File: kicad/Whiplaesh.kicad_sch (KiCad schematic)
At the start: 74 parts, among them SW1 SW_PUSH, SW10 SW_PUSH, SW11 SW_PUSH, SW12 SW_PUSH, SW13 SW_PUSH, SW14 SW_PUSH, SW15 SW_PUSH, SW16 SW_PUSH, SW17 SW_PUSH, SW18 SW_PUSH, SW19 SW_PUSH, SW2 SW_PUSH, SW20 SW_PUSH, SW21 SW_PUSH, SW22 SW_PUSH, SW23 SW_PUSH, SW24 SW_PUSH, SW25 SW_PUSH, SW26 SW_PUSH, SW27 SW_PUSH, SW28 SW_PUSH, SW29 SW_PUSH, SW3 SW_PUSH, SW30 SW_PUSH, SW31 SW_PUSH, SW32 SW_PUSH, SW4 SW_PUSH, SW5 SW_PUSH, SW6 SW_PUSH, SW7 SW_PUSH, SW8 SW_PUSH, SW9 SW_PUSH

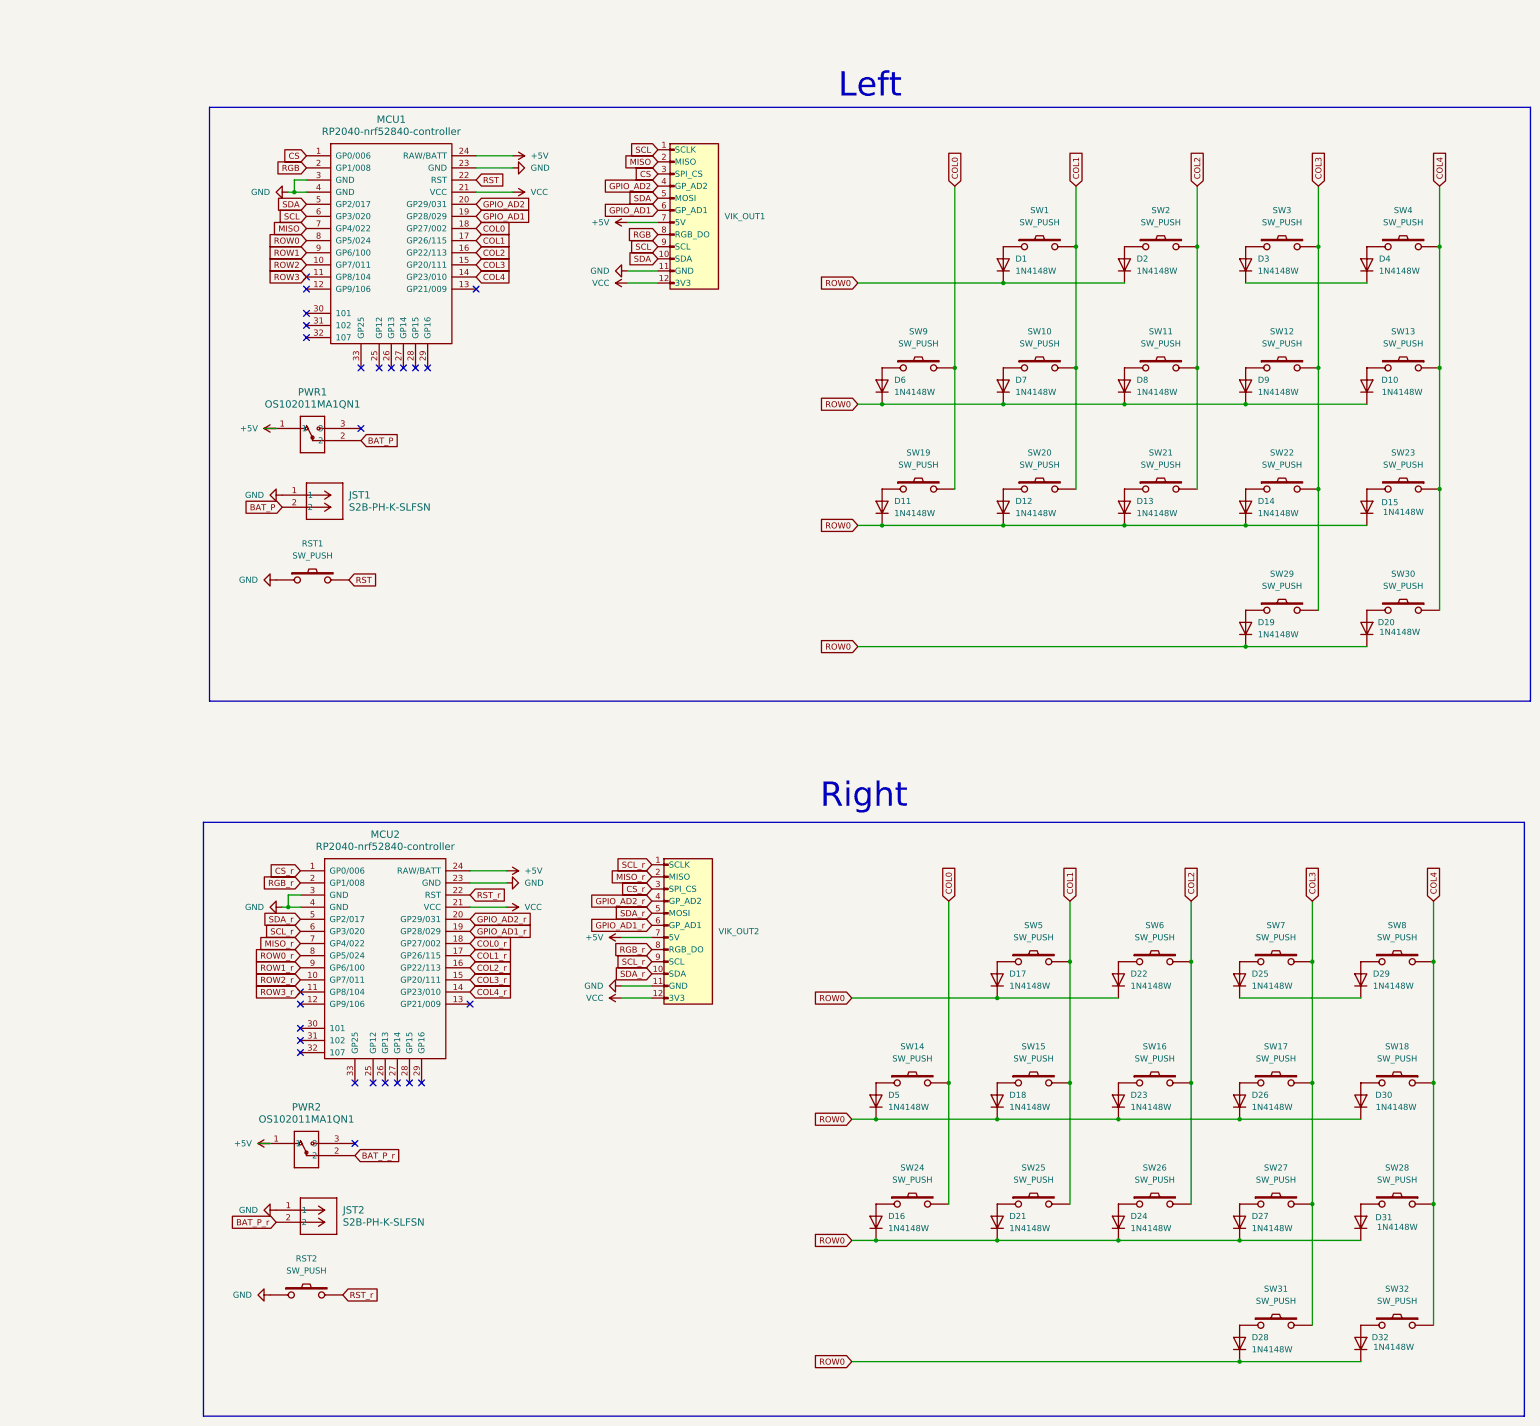
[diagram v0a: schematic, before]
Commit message: Add missing connections, fix diodes references, fix shared pins on vik connector
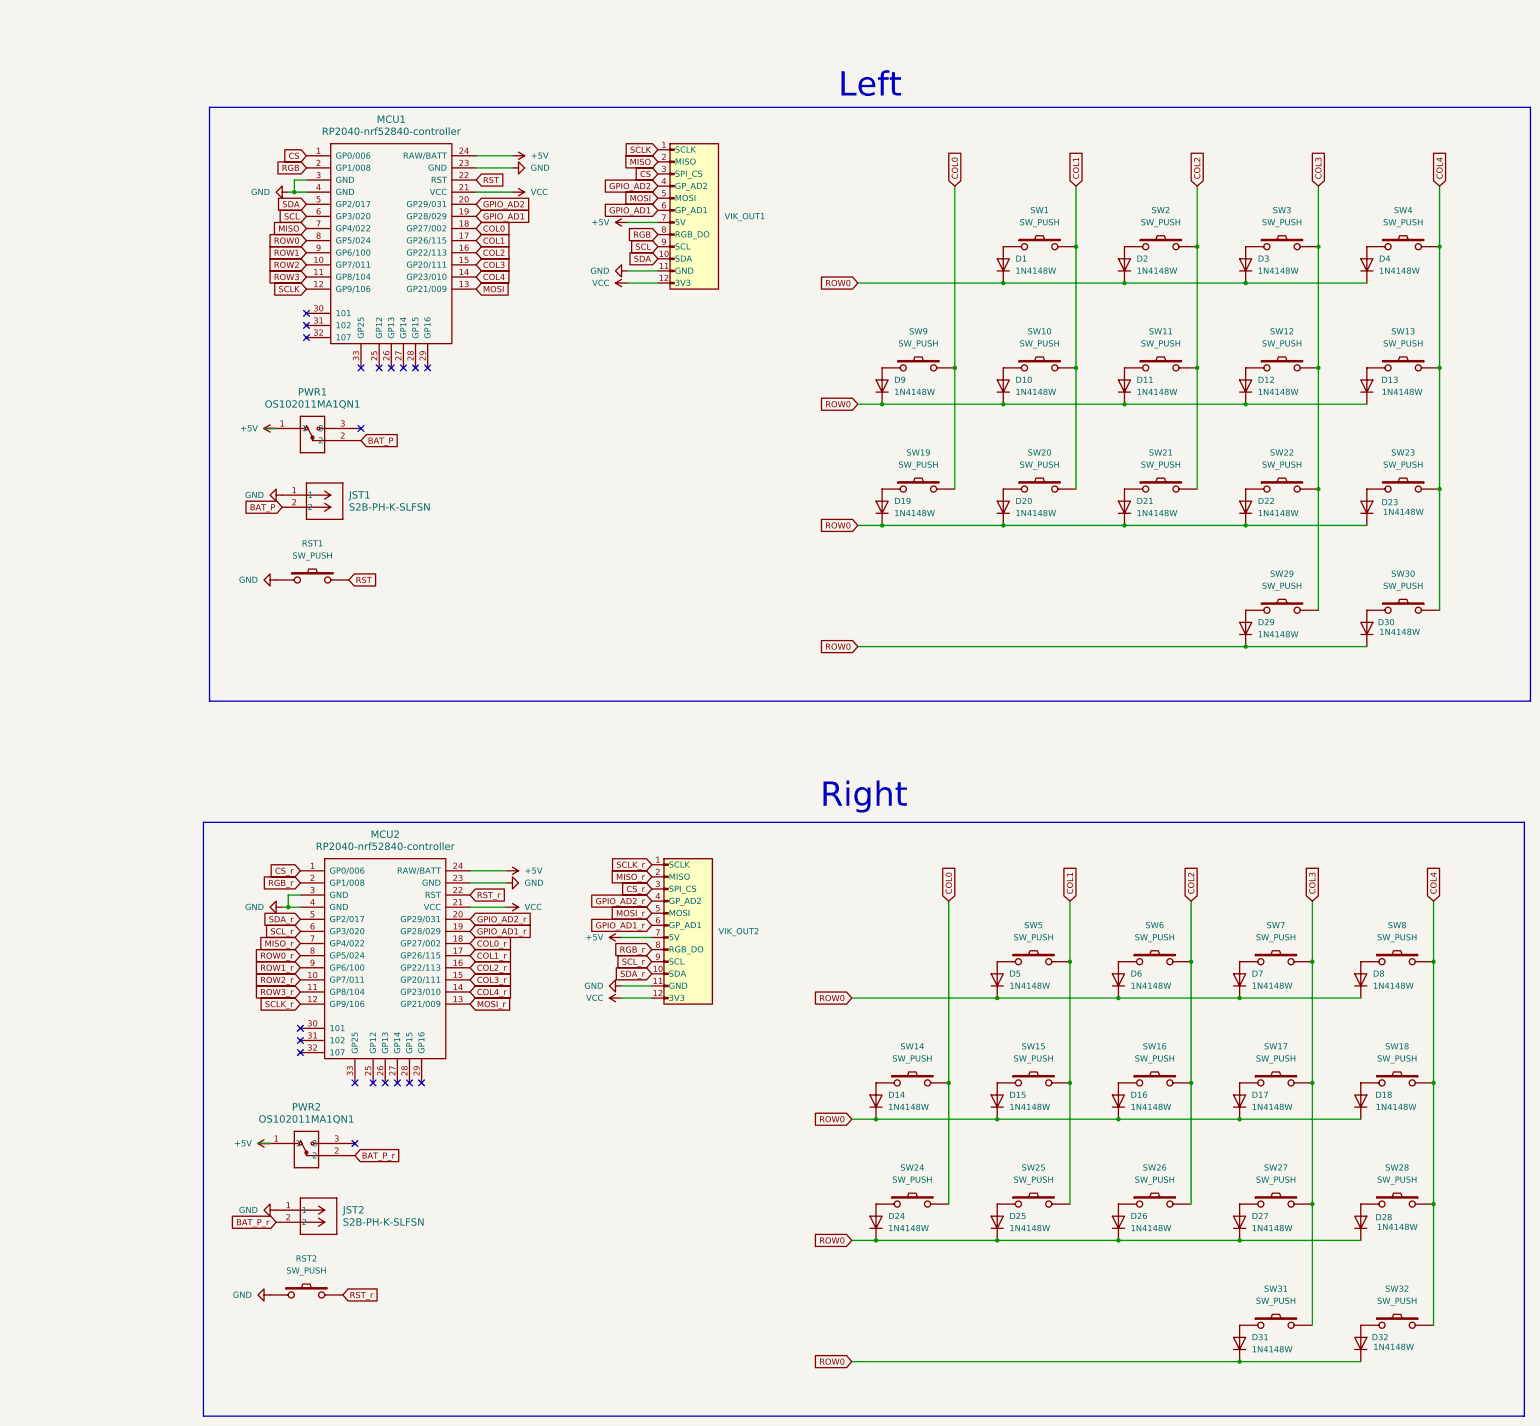
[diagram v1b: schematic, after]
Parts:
- renumbered D7 to D10, D8 to D11, D9 to D12, D10 to D13, D5 to D14, D18 to D15, D23 to D16, D26 to D17, D30 to D18, D11 to D19, D12 to D20, D13 to D21, D14 to D22, D15 to D23, D16 to D24, D21 to D25, D24 to D26, D31 to D28, D19 to D29, D20 to D30, D28 to D31, D17 to D5, D22 to D6, D25 to D7, D29 to D8, D6 to D9
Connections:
- net ROW0: now also D3.1 (K), D4.1 (K), D7.1 (K), D8.1 (K)
- net SCL: no longer VIK_OUT1.1 (SCLK)
- net SCL_r: no longer VIK_OUT2.1 (SCLK)
- net SDA: no longer VIK_OUT1.5 (MOSI)
- net SDA_r: no longer VIK_OUT2.5 (MOSI)
- net SCLK_r: now reaches MCU2.12 (GP9/106)
- net SCLK_r: now also VIK_OUT2.1 (SCLK)
- net MOSI_r: now reaches MCU2.13 (GP21/009)
- net MOSI_r: now also VIK_OUT2.5 (MOSI)
- net SCLK: now reaches MCU1.12 (GP9/106)
- net SCLK: now also VIK_OUT1.1 (SCLK)
- net MOSI: now reaches MCU1.13 (GP21/009)
- net MOSI: now also VIK_OUT1.5 (MOSI)
- no-connect marks 26 -> 20

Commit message: Separate left and right, add kicad footprints and symbols
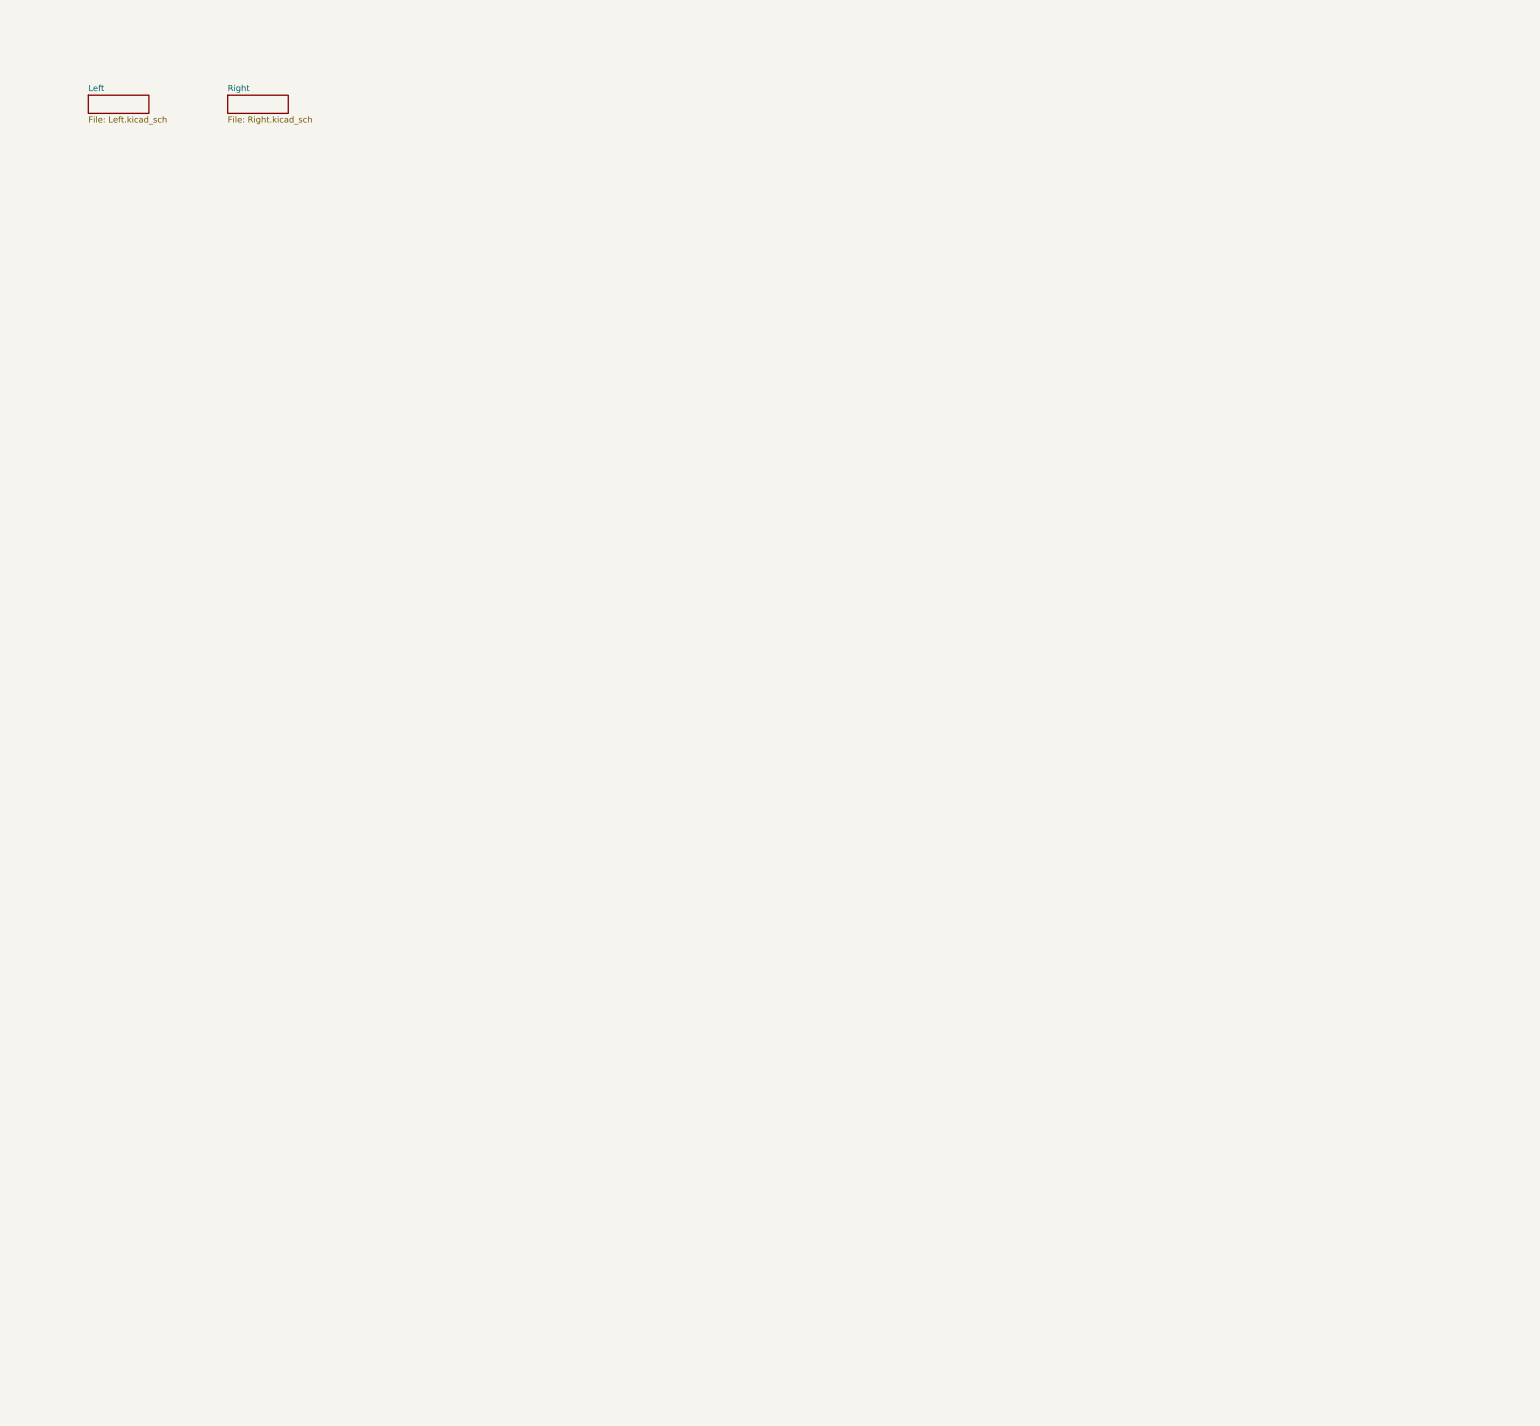
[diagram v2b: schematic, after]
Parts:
- removed D1, D10, D11, D12, D13, D14, D15, D16, D17, D18, D19, D2, D20, D21, D22, D23, D24, D25, D26, D27, D28, D29, D3, D30, D31, D32, D4, D5, D6, D7, D8, D9: 1N4148W, Diode_SMD:D_SOD-123, symbol Diode:1N4148W
- removed JST1, JST2: S2B-PH-K-SLFSN, CONN_S2B-PH-K-S_JST, symbol CONN_S2B-PH-K-S_JST:S2B-PH-K-SLFSN
- removed MCU1, MCU2: RP2040-nrf52840-controller, symbol RP2040-nrf52840-controller:RP2040-nrf52840-controller
- removed PWR1, PWR2: OS102011MA1QN1, OS102011MA1QN1_CNK, symbol 2024-10-29_23-28-51:OS102011MA1QN1
- removed RST1, RST2, SW1, SW10, SW11, SW12, SW13, SW14, SW15, SW16, SW17, SW18, SW19, SW2, SW20, SW21, SW22, SW23, SW24, SW25, SW26, SW27, SW28, SW29, SW3, SW30, SW31, SW32, SW4, SW5, SW6, SW7, SW8, SW9: SW_PUSH, symbol kbd:SW_PUSH
- removed VIK_OUT1, VIK_OUT2: vik-module-connector, symbol vik:vik-module-connector
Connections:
- no-connect marks 20 -> 0
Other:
- added sheet Left (Left.kicad_sch)
- added sheet Right (Right.kicad_sch)
- note removed: "Left"
- note removed: "Right"
- title: Whiplaesh -> (none)
